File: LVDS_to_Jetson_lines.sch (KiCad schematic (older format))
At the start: 21 parts, among them U2 SN74AVC2T45DCUR, U5 TS3DDR3812_RUA_42, U6 TS3DDR3812_RUA_42, U8 SN74AVCH16T245_DGV_48

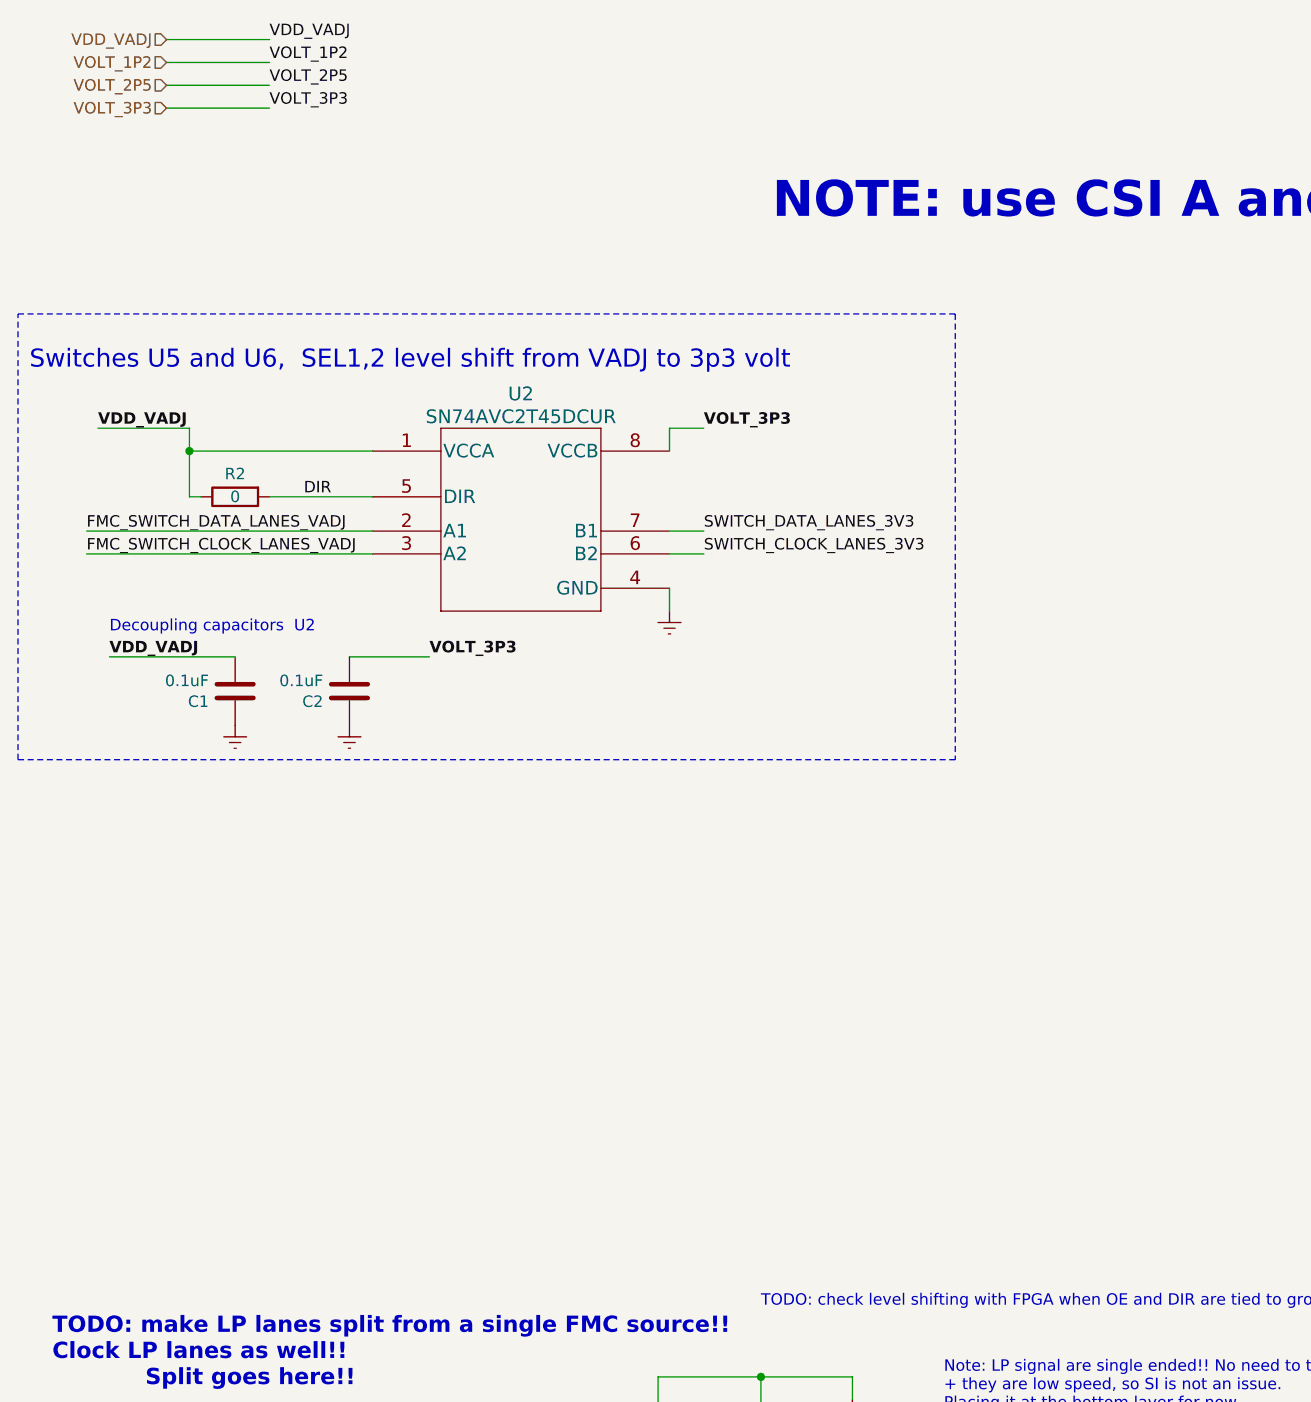
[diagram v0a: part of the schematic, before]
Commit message: added more level shifters and power 1.8 Volt
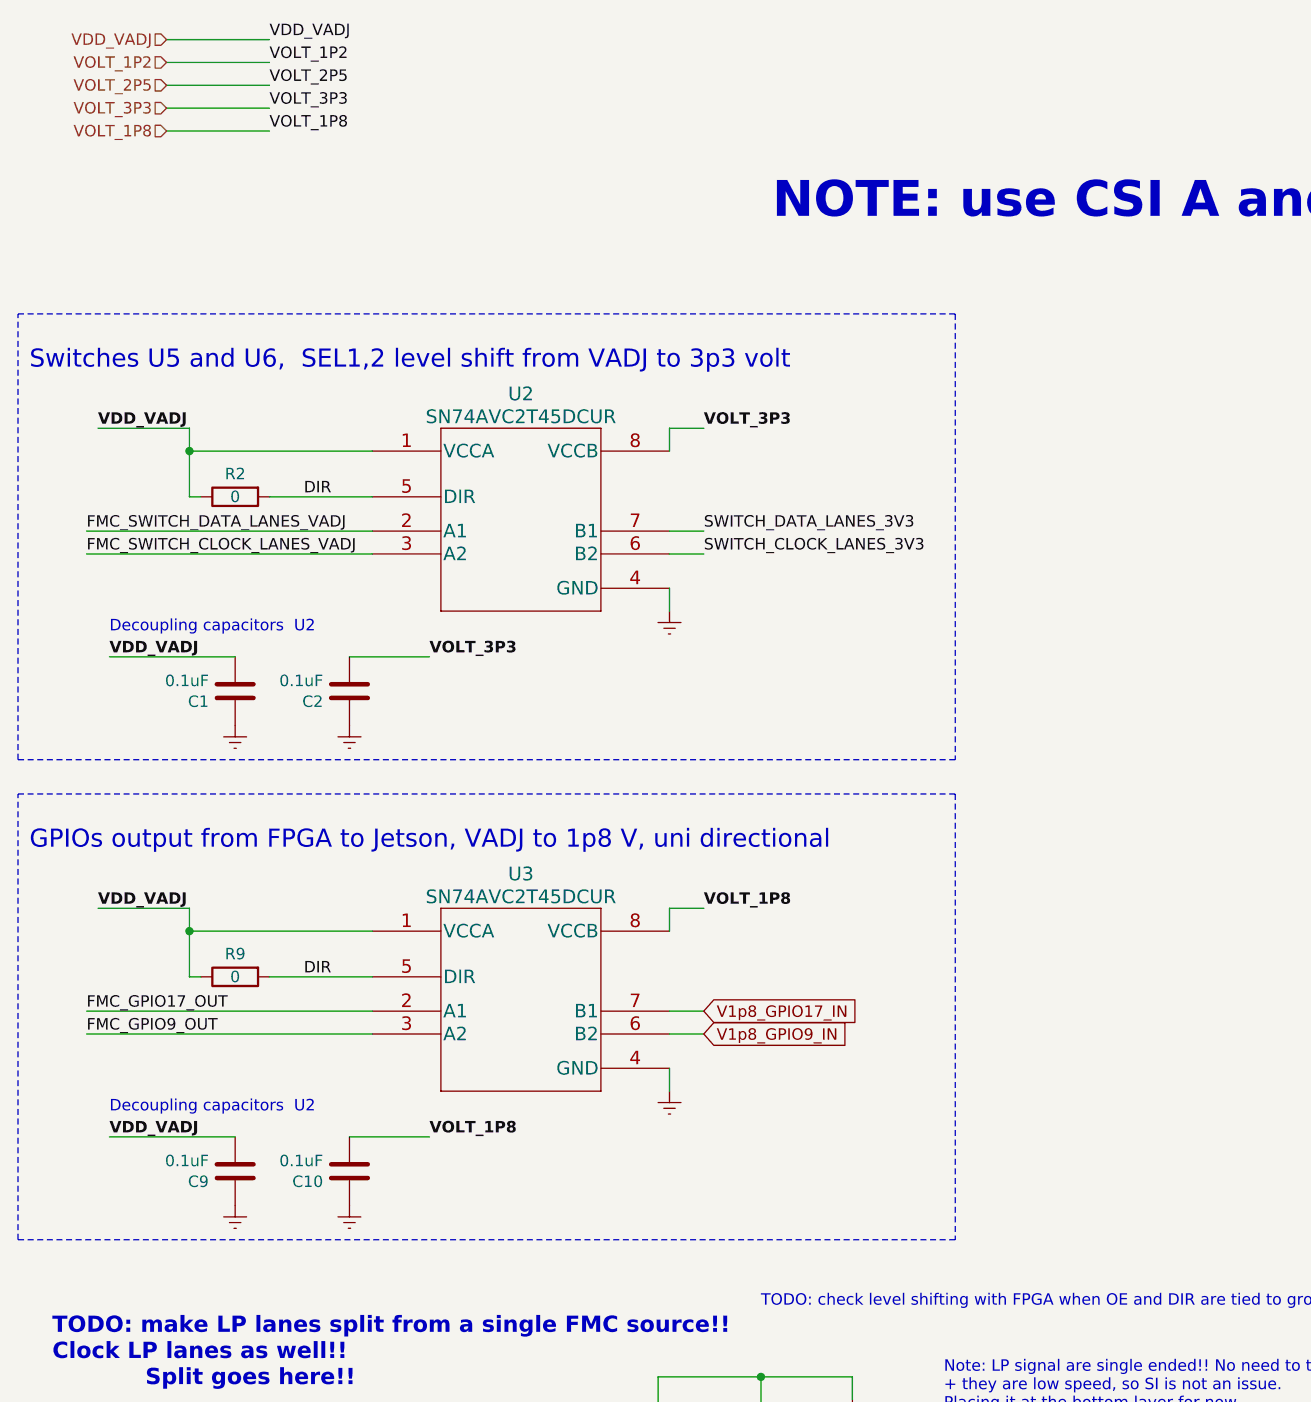
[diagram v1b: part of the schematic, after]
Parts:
- added C10, C9: 0.1uF, Capacitors_SMD:C_0402, symbol FMC_MIPI_v2:C
- added R9: 0, Resistors_SMD:R_0805, symbol Device:R
- added U3: SN74AVC2T45DCUR, FMC_MIPI_v2_sym:SN74AVC2T45DCUR, symbol FMC_MIPI_v2:SN74AVC2T45DCUR
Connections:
- net labels added: FMC_GPIO17_OUT, FMC_GPIO9_OUT, V1p8_GPIO17_IN, V1p8_GPIO9_IN, VOLT_1P8
- wire segments 269 -> 285
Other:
- note added: "GPIOs output from FPGA to Jetson, VADJ to 1p8 V, uni directional"

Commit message: minor changes 4
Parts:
- removed C10, C9: 0.1uF, Capacitors_SMD:C_0402, symbol FMC_MIPI_v2:C
- removed R9: 0, Resistors_SMD:R_0805, symbol Device:R
- removed U3: SN74AVC2T45DCUR, FMC_MIPI_v2_sym:SN74AVC2T45DCUR, symbol FMC_MIPI_v2:SN74AVC2T45DCUR
- added R10: 4.7k, Resistors_SMD:R_0805, symbol Device:R
- R2: value 0 -> 4.7k; Part Number RC0805JR-070RL -> CR0805-JW-472ELF
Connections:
- net labels added: DIR_U2, DIR_U8
- net labels removed: DIR, FMC_GPIO17_OUT, FMC_GPIO9_OUT, V1p8_GPIO17_IN, V1p8_GPIO9_IN
- wire segments 285 -> 271
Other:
- note added: "Note: LP signal are single ended!! No need to treat them as diffrential,\n+ they are low speed, so SI is not an issue.\nPlacing it at the bottom layer for now.\nB -> A switching time = 2.9 ns\nA -> B switching time = 2.6"
- note removed: "GPIOs output from FPGA to Jetson, VADJ to 1p8 V, uni directional"
- note removed: "Note: LP signal are single ended!! No need to treat them as diffrential,\n+ they are low speed, so SI is not an issue.\nPlacing it at the bottom layer for now."

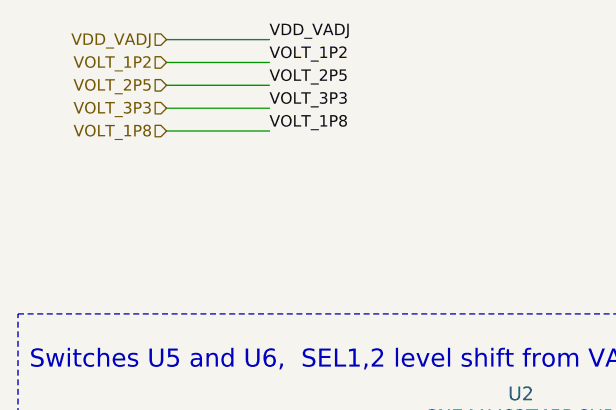
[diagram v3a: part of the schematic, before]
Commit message: adding more power supplies
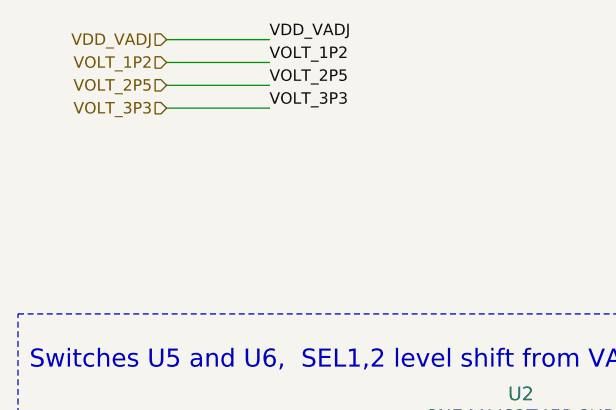
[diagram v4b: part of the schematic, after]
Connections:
- net labels removed: VOLT_1P8
- wire segments 271 -> 270
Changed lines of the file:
@@
 Text Label 1900 2650 0    50   ~ 0
 DIR_U2
-Text HLabel 1300 1050 0    50   Input ~ 0
-VOLT_1P8
-Wire Wire Line
-	1300 1050 1750 1050
-Text Label 1750 1050 0    50   ~ 0
-VOLT_1P8
 Wire Wire Line
 	3200 9600 3200 10200
